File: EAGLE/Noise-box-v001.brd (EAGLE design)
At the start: 80.5 x 40.1 mm, 76 parts, among them J1 AVR_SPI_PROG_3X22X3_LOCK, J4 MICRO-SD_CARD_SOCKET, J5 HEADPHONE, J6 POWER_JACK, U1 ATMEGA328P_TQFP, U2 MIC5219 3.3V, U3 MCP73831, Y1 12.288MHz, Y2 8MHz

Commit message: Triggers
Added momentary buttons to act as triggers. These will choose between
music categories, songs, or other user input features.
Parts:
- added S10: MOMENTARY-SWITCH-SPST-SMD-4.5MM, SparkFun-Switches:TACTILE_SWITCH_SMD_4.5MM
- added S4: (no value), SparkFun-Switches:ENCODER_LED_3
- added S5: 1, SparkFun-Switches:TACTILE_SWITCH_SMD_4.5MM
- added S6: 2, SparkFun-Switches:TACTILE_SWITCH_SMD_4.5MM
- added S7: 3, SparkFun-Switches:TACTILE_SWITCH_SMD_4.5MM
- added S8: 4, SparkFun-Switches:TACTILE_SWITCH_SMD_4.5MM
- added S9: 5, SparkFun-Switches:TACTILE_SWITCH_SMD_4.5MM
- S2, S3: device SparkFun-Switches:TACTILE_SWITCH_PTH_6.0MM -> SparkFun-Switches:TACTILE_SWITCH_SMD_4.5MM
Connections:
- net N$23 renamed ROT-LEDR
- net N$28 renamed ROT-LEDB
- net N$29 renamed ROT-SW
- net N$30 renamed ROT-A
- net N$38 renamed ROT-B
- net N$40 renamed ROT-LEDG
- removed net N$32: U1.31
- removed net N$33: U1.30
- removed net N$36: U1.28
- removed net N$37: U1.27
- removed net N$41: U1.23
- new net TRIG1: S5.2, S5.3, U1.23
- new net TRIG2: S6.2, S6.3, U1.27
- new net TRIG3: S7.2, S7.3, U1.28
- new net TRIG4/TXO: S8.2, S8.3, U1.31
- new net TRIG5/RXI: S9.2, S9.3, U1.30
- net GND: now also S2.2, S2.3, S3.2, S3.3, S5.1, S5.4, S6.1, S6.4, S7.1, S7.4, S8.1, S8.4, S9.1, S9.4; no longer S2.1, S3.1
- net N$43: now also S3.1, S3.4; no longer S3.3
- net N$44: now also S2.1, S2.4; no longer S2.3
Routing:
- net N$44: track 21.9 -> 28.6 mm
- net N$43: track 14.3 -> 20.6 mm
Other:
- board size 80.5 x 40.1 mm -> 80.5 x 52.1 mm
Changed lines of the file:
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@@
 <board>
 <plain>
-<wire x1="-2.032" y1="42.672" x2="78.486" y2="42.672" width="0.254" layer="20"/>
-<wire x1="78.486" y1="42.672" x2="78.486" y2="2.54" width="0.254" layer="20"/>
+<wire x1="-2.032" y1="54.61" x2="78.486" y2="54.61" width="0.254" layer="20"/>
+<wire x1="78.486" y1="54.61" x2="78.486" y2="2.54" width="0.254" layer="20"/>
 <wire x1="78.486" y1="2.54" x2="-2.032" y2="2.54" width="0.254" layer="20"/>
-<wire x1="-2.032" y1="2.54" x2="-2.032" y2="42.672" width="0.254" layer="20"/>
+<wire x1="-2.032" y1="2.54" x2="-2.032" y2="54.61" width="0.254" layer="20"/>
 </plain>
 <attributes>
@@
 <attribute name="PROD_ID" value="CAP-08604" x="16.256" y="19.05" size="1.778" layer="27" display="off"/>
 </element>
-<element name="S2" library="SparkFun-Switches" package="TACTILE_SWITCH_PTH_6.0MM" value="UP" x="16.764" y="6.604" rot="R180">
-<attribute name="SF_SKU" value="COM-00097" x="16.764" y="6.604" size="1.778" layer="27" rot="R180" display="off"/>
-<attribute name="PROD_ID" value=" SWCH-08441" x="16.764" y="6.604" size="1.778" layer="27" rot="R180" display="off"/>
-</element>
-<element name="S3" library="SparkFun-Switches" package="TACTILE_SWITCH_PTH_6.0MM" value="DOWN" x="16.764" y="13.716" rot="R180">
-<attribute name="SF_SKU" value="COM-00097" x="16.764" y="13.716" size="1.778" layer="27" rot="R180" display="off"/>
-<attribute name="PROD_ID" value=" SWCH-08441" x="16.764" y="13.716" size="1.778" layer="27" rot="R180" display="off"/>
+<element name="S2" library="SparkFun-Switches" package="TACTILE_SWITCH_SMD_4.5MM" value="UP" x="16.764" y="6.604" rot="R180">
+<attribute name="PROD_ID" value="SWCH-09213" x="16.764" y="6.604" size="1.778" layer="27" rot="R180" display="off"/>
+</element>
+<element name="S3" library="SparkFun-Switches" package="TACTILE_SWITCH_SMD_4.5MM" value="DOWN" x="16.764" y="13.716" rot="R180">
+<attribute name="PROD_ID" value="SWCH-09213" x="16.764" y="13.716" size="1.778" layer="27" rot="R180" display="off"/>
 </element>
 <element name="J2" library="SparkFun-Connectors" package="1X02_2.54_SCREWTERM" value="" x="26.416" y="6.858" rot="R180"/>
@@
 <element name="R18" library="SparkFun-Resistors" package="0603" value="10k" x="55.626" y="8.382" rot="MR0">
 <attribute name="PROD_ID" value="RES-00824" x="55.626" y="8.382" size="1.778" layer="28" rot="MR0" display="off"/>
+</element>
+<element name="S4" library="SparkFun-Switches" package="ENCODER_LED_3" value="" x="-51.308" y="50.8">
+<attribute name="SF_SKU" value="COM-10982" x="-51.308" y="50.8" size="1.778" layer="27" display="off"/>
+<attribute name="PROD_ID" value="RES-10859" x="-51.308" y="50.8" size="1.778" layer="27" display="off"/>
+</element>
+<element name="S5" library="SparkFun-Switches" package="TACTILE_SWITCH_SMD_4.5MM" value="1" x="38.354" y="45.466">
+<attribute name="PROD_ID" value="SWCH-09213" x="38.354" y="45.466" size="1.778" layer="27" display="off"/>
+</element>
+<element name="S6" library="SparkFun-Switches" package="TACTILE_SWITCH_SMD_4.5MM" value="2" x="44.45" y="45.466">
+<attribute name="PROD_ID" value="SWCH-09213" x="44.45" y="45.466" size="1.778" layer="27" display="off"/>
+</element>
+<element name="S7" library="SparkFun-Switches" package="TACTILE_SWITCH_SMD_4.5MM" value="3" x="50.546" y="45.466">
+<attribute name="PROD_ID" value="SWCH-09213" x="50.546" y="45.466" size="1.778" layer="27" display="off"/>
+</element>
+<element name="S8" library="SparkFun-Switches" package="TACTILE_SWITCH_SMD_4.5MM" value="4" x="56.388" y="45.466">
+<attribute name="PROD_ID" value="SWCH-09213" x="56.388" y="45.466" size="1.778" layer="27" display="off"/>
+</element>
+<element name="S9" library="SparkFun-Switches" package="TACTILE_SWITCH_SMD_4.5MM" value="5" x="62.484" y="45.466">
+<attribute name="PROD_ID" value="SWCH-09213" x="62.484" y="45.466" size="1.778" layer="27" display="off"/>
+</element>
+<element name="S10" library="SparkFun-Switches" package="TACTILE_SWITCH_SMD_4.5MM" value="MOMENTARY-SWITCH-SPST-SMD-4.5MM" x="-66.802" y="51.562">
+<attribute name="PROD_ID" value="SWCH-09213" x="-66.802" y="51.562" size="1.778" layer="27" display="off"/>
 </element>
 </elements>
@@
 <contactref element="C23" pad="2"/>
 <contactref element="C22" pad="2"/>
-<contactref element="S2" pad="1"/>
-<contactref element="S3" pad="1"/>
+<contactref element="S2" pad="2"/>
+<contactref element="S3" pad="2"/>
 <contactref element="J6" pad="GNDBREAK"/>
 <contactref element="BT2" pad="GND@1"/>
@@
 <wire x1="20.864" y1="35.088" x2="20.828" y2="35.052" width="0.254" layer="1"/>
 <polygon width="0.254" layer="1">
-<vertex x="-4.064" y="46.482"/>
-<vertex x="83.312" y="46.482"/>
-<vertex x="83.312" y="-0.762"/>
+<vertex x="-4.064" y="66.04"/>
+<vertex x="87.122" y="66.04"/>
+<vertex x="87.122" y="-0.762"/>
 <vertex x="-4.064" y="-0.762"/>
 </polygon>
 <polygon width="0.254" layer="16">
-<vertex x="-2.286" y="50.038"/>
-<vertex x="81.788" y="50.038"/>
+<vertex x="-8.128" y="62.992"/>
+<vertex x="81.788" y="62.992"/>
 <vertex x="81.788" y="0.508"/>
-<vertex x="-2.286" y="0.508"/>
+<vertex x="-8.128" y="0.508"/>
 </polygon>
+<contactref element="S2" pad="3"/>
+<contactref element="S3" pad="3"/>
+<contactref element="S5" pad="1"/>
+<contactref element="S5" pad="4"/>
+<contactref element="S6" pad="1"/>
+<contactref element="S6" pad="4"/>
+<contactref element="S7" pad="1"/>
+<contactref element="S7" pad="4"/>
+<contactref element="S8" pad="1"/>
+<contactref element="S8" pad="4"/>
+<contactref element="S9" pad="1"/>
+<contactref element="S9" pad="4"/>
 <wire x1="27.364" y1="33.754" x2="27.364" y2="33.254" width="0" layer="19" extent="1-1"/>
 <wire x1="27.364" y1="32.754" x2="27.364" y2="33.254" width="0" layer="19" extent="1-1"/>
@@
 <wire x1="41.396" y1="35.255" x2="40.583" y2="36.068" width="0.254" layer="1"/>
 </signal>
-<signal name="N$23">
+<signal name="ROT-LEDR">
 <contactref element="U1" pad="14"/>
 </signal>
-<signal name="N$28">
+<signal name="ROT-LEDB">
 <contactref element="U1" pad="9"/>
 </signal>
-<signal name="N$29">
+<signal name="ROT-SW">
 <contactref element="U1" pad="2"/>
 </signal>
-<signal name="N$30">
+<signal name="ROT-A">
 <contactref element="U1" pad="1"/>
 </signal>
-<signal name="N$32">
+<signal name="TRIG4/TXO">
 <contactref element="U1" pad="31"/>
-</signal>
-<signal name="N$33">
+<contactref element="S8" pad="2"/>
+<contactref element="S8" pad="3"/>
+<wire x1="54.163" y1="43.716" x2="58.613" y2="43.716" width="0" layer="19" extent="1-1"/>
+<wire x1="48.4886" y1="31.972" x2="54.163" y2="43.716" width="0" layer="19" extent="1-1"/>
+</signal>
+<signal name="TRIG5/RXI">
 <contactref element="U1" pad="30"/>
-</signal>
-<signal name="N$36">
+<contactref element="S9" pad="2"/>
+<contactref element="S9" pad="3"/>
+<wire x1="60.259" y1="43.716" x2="64.709" y2="43.716" width="0" layer="19" extent="1-1"/>
+<wire x1="48.4886" y1="31.172" x2="60.259" y2="43.716" width="0" layer="19" extent="1-1"/>
+</signal>
+<signal name="TRIG3">
 <contactref element="U1" pad="28"/>
-</signal>
-<signal name="N$37">
+<contactref element="S7" pad="2"/>
+<contactref element="S7" pad="3"/>
+<wire x1="48.321" y1="43.716" x2="52.771" y2="43.716" width="0" layer="19" extent="1-1"/>
+<wire x1="48.4886" y1="29.572" x2="48.321" y2="43.716" width="0" layer="19" extent="1-1"/>
+</signal>
+<signal name="TRIG2">
 <contactref element="U1" pad="27"/>
-</signal>
-<signal name="N$38">
+<contactref element="S6" pad="2"/>
+<contactref element="S6" pad="3"/>
+<wire x1="42.225" y1="43.716" x2="46.675" y2="43.716" width="0" layer="19" extent="1-1"/>
+<wire x1="48.4886" y1="28.772" x2="46.675" y2="43.716" width="0" layer="19" extent="1-1"/>
+</signal>
+<signal name="ROT-B">
 <contactref element="U1" pad="26"/>
 </signal>
-<signal name="N$40">
+<signal name="ROT-LEDG">
 <contactref element="U1" pad="24"/>
 </signal>
-<signal name="N$41">
+<signal name="TRIG1">
 <contactref element="U1" pad="23"/>
+<contactref element="S5" pad="2"/>
+<contactref element="S5" pad="3"/>
+<wire x1="36.129" y1="43.716" x2="40.579" y2="43.716" width="0" layer="19" extent="1-1"/>
+<wire x1="46.196" y1="25.6794" x2="40.579" y2="43.716" width="0" layer="19" extent="1-1"/>
 </signal>
 <signal name="N$24">
@@
 <signal name="N$43">
 <contactref element="U$4" pad="5"/>
-<contactref element="S3" pad="3"/>
-<wire x1="20.0152" y1="15.9766" x2="20.0152" y2="17.4752" width="0.254" layer="16"/>
+<contactref element="S3" pad="1"/>
+<wire x1="14.539" y1="11.966" x2="20.0152" y2="17.4752" width="0.254" layer="16"/>
 <wire x1="20.0152" y1="17.4752" x2="20.574" y2="18.034" width="0.254" layer="16"/>
 <wire x1="20.574" y1="18.034" x2="26.924" y2="18.034" width="0.254" layer="16"/>
@@
 <wire x1="27.432" y1="22.098" x2="27.432" y2="21.215" width="0.254" layer="1"/>
 <wire x1="27.432" y1="21.215" x2="27.813" y2="20.834" width="0.254" layer="1"/>
+<contactref element="S3" pad="4"/>
+<wire x1="14.539" y1="11.966" x2="18.989" y2="11.966" width="0" layer="19" extent="1-1"/>
+<wire x1="14.539" y1="11.966" x2="14.539" y2="11.966" width="0" layer="19" extent="1-16"/>
 </signal>
 <signal name="N$44">
 <contactref element="U$4" pad="4"/>
-<contactref element="S2" pad="3"/>
-<wire x1="20.0152" y1="8.8646" x2="20.2946" y2="8.8646" width="0.254" layer="16"/>
+<contactref element="S2" pad="1"/>
+<wire x1="14.539" y1="4.854" x2="20.2946" y2="8.8646" width="0.254" layer="16"/>
 <wire x1="20.2946" y1="8.8646" x2="21.59" y2="10.16" width="0.254" layer="16"/>
 <wire x1="21.59" y1="10.16" x2="21.59" y2="16.764" width="0.254" layer="16"/>
@@
 <wire x1="29.21" y1="21.844" x2="29.21" y2="20.961" width="0.254" layer="1"/>
 <wire x1="29.21" y1="20.961" x2="29.083" y2="20.834" width="0.254" layer="1"/>
+<contactref element="S2" pad="4"/>
+<wire x1="20.2946" y1="8.8646" x2="18.989" y2="4.854" width="0" layer="19" extent="1-16"/>
+<wire x1="14.539" y1="4.854" x2="14.539" y2="4.854" width="0" layer="19" extent="1-16"/>
 </signal>
 <signal name="AMP-SHDN">

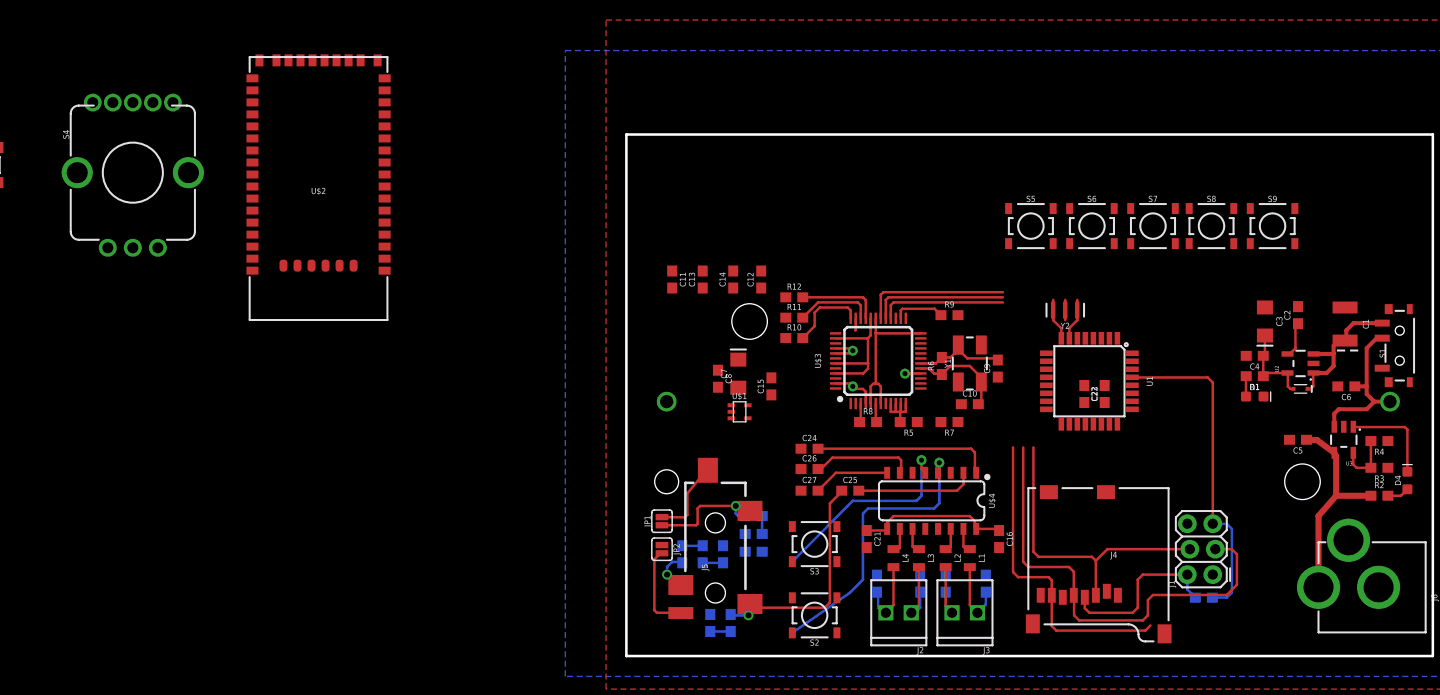
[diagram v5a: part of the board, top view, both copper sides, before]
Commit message: More layout, buttons, debug header
Added a handful of buttons and a rotary switch to handle user inputs
such a track selection, volume knob, pause/play, etc. Added 5 pin debug
header for FTDI to USB adapter I have. Advanced the layout - nearly
complete.
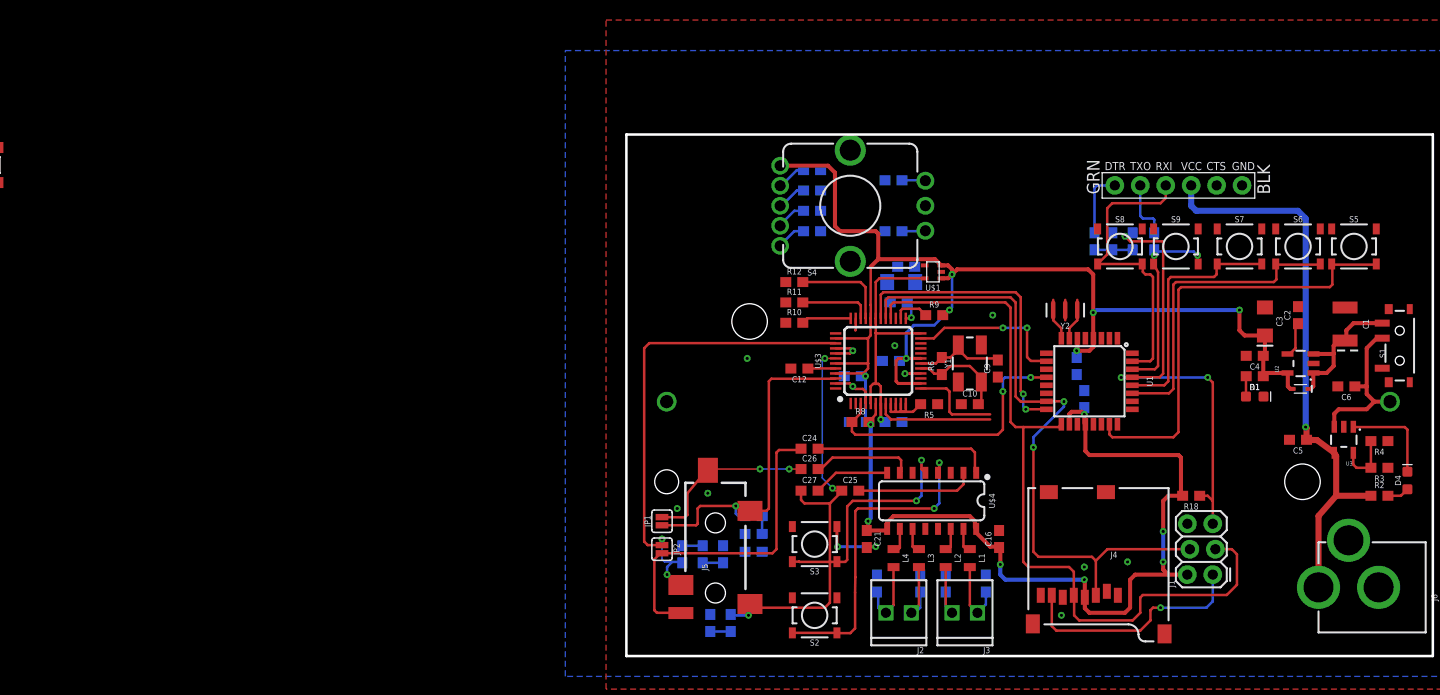
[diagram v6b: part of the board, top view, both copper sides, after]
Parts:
- removed U$2: BLUETOOTH-RN-52, SparkFun-RF:RN-52
- added C31, C32, C33: 0.1uF, SparkFun-Capacitors:0603
- added J7: (no value), SparkFun-Connectors:6_PIN_SERIAL_TARGET_SIDE_W_SILK
- added R19, R20, R21: 330, SparkFun-Resistors:0603
- added R22, R23: 1k, SparkFun-Resistors:0603
- added R25: 10k, SparkFun-Resistors:0603
- added R26: 2.0k, SparkFun-Resistors:0603
- moved S4 71.7 mm to (20.3, 47.5), turned to 90 degrees
- moved S5 32.3 mm to (70.6, 43.4)
- moved U$1 23.8 mm to (28.6, 40.9), turned to 90 degrees
- moved C11 23.3 mm to (24.4, 32.0), flipped to the bottom, turned to 0 degrees
- moved C8 21.9 mm to (25.9, 41.4), flipped to the bottom, turned to 0 degrees
- moved S6 20.7 mm to (65.0, 43.4)
- moved C14 18.9 mm to (21.1, 25.9), flipped to the bottom, turned to 0 degrees
- moved C7 18.7 mm to (25.4, 39.9), flipped to the bottom, turned to 180 degrees
- moved C13 17.8 mm to (20.6, 30.5), flipped to the bottom, turned to 0 degrees
- moved R7 13.0 mm to (25.1, 37.8), flipped to the bottom
- moved C15 12.7 mm to (24.6, 25.9), flipped to the bottom, turned to 180 degrees
- moved R18 10.2 mm to (54.4, 18.5), flipped to the top, turned to 180 degrees
- moved S9 9.86 mm to (52.8, 43.4)
- moved C12 9.67 mm to (15.2, 31.2), turned to 180 degrees
- moved S8 9.37 mm to (47.2, 43.4)
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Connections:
- new net DTR: J7.P$1, R23.1
- new net N$26: C33.1, R23.2, R26.1
- new net N$28: R22.2, S4.3
- new net N$29: R19.2, S4.4
- new net N$30: R20.2, S4.2
- new net N$31: R21.2, S4.1
- new net RXI: J7.P$2, R25.2
- net +3V3: now also S4.5
- net GND: now also C31.2, C32.2, J7.P$5, J7.P$6, R22.1, R26.2, S4.C
- net ROT-A: now also C32.1, S4.A
- net ROT-B: now also C31.1, S4.B
- net ROT-LEDB: now also R19.1
- net ROT-LEDG: now also R20.1
- net ROT-LEDR: now also R21.1
- net RST: now also C33.2
- net TRIG4/TXO: now also J7.P$3
- net TRIG5/RXI: now also R25.1
- net VIN: now also J7.P$4
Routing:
- net +3V3: track 58.0 -> 215.5 mm, vias 0 -> 14
- net TRIG1: track 0.00 -> 44.5 mm
- net RIGHT: track 4.34 -> 48.7 mm, vias 1 -> 2
- net VIN: track 20.8 -> 56.9 mm, vias 0 -> 1
- net TRIG2: track 0.00 -> 31.2 mm
- net TRIG4/TXO: track 0.00 -> 30.3 mm
- net MP3-RST: track 1.96 -> 28.0 mm, vias 0 -> 2
- net TRIG3: track 0.00 -> 24.5 mm
- net AMP-R: track 8.86 -> 32.7 mm
- net MOSI: track 44.0 -> 65.8 mm, vias 0 -> 2
- net LEFT: track 12.5 -> 33.9 mm
- net TRIG5/RXI: track 0.00 -> 20.0 mm, vias 0 -> 2
- net SCK: track 58.1 -> 78.0 mm
- net GBUF: track 23.0 -> 42.6 mm, vias 1 -> 3
- net MP3-CS: track 0.00 -> 16.1 mm, vias 0 -> 2
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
